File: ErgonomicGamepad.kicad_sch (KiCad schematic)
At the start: 68 parts, among them J1 USB_C_Receptacle_USB2.0_16P, J2 Conn_01x08, J3 Conn_01x08, J4 Conn_01x08, J5 AVR-ISP-6, J6 Conn_01x08, SW09 SW_DIP_x01, SW1 SW_DIP_x01, SW10 SW_DIP_x01, SW11 SW_DIP_x01, SW12 SW_DIP_x01, SW13 SW_DIP_x01, SW14 SW_DIP_x01, SW15 SW_DIP_x01, SW16 SW_DIP_x01, SW17 SW_DIP_x01, SW18 SW_DIP_x01, SW19 SW_DIP_x01, SW2 SW_DIP_x01, SW20 SW_DIP_x01, SW21 SW_DIP_x01, SW22 SW_DIP_x01, SW23 SW_DIP_x01, SW24 SW_DIP_x01, SW3 SW_DIP_x01, SW4 SW_DIP_x01, SW5 SW_DIP_x01, SW6 SW_DIP_x01, SW7 SW_DIP_x01, SW8 SW_DIP_x01, U1 ATmega32U4-A, Y1 Crystal

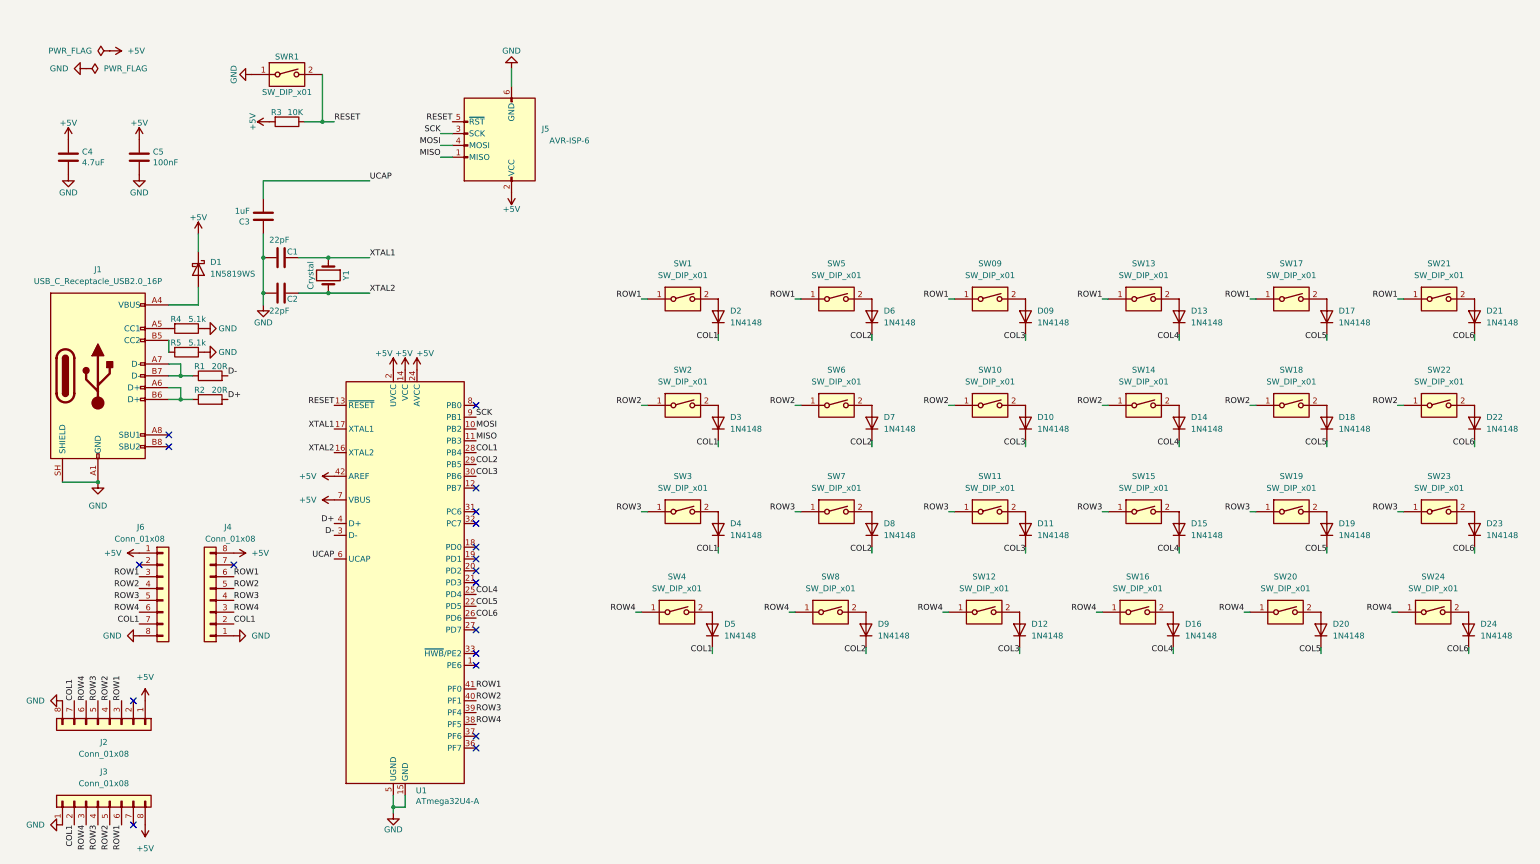
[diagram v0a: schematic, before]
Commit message: Assign footprints, fix RESET wiring, select JLCPCB as vendor
- Selected JLCPCB (+ LCSC parts catalog) as fabrication/assembly vendor
- Assigned footprints to 82 of 83 components (all but SWR1 reset
  switch, pending real pad dimensions from its datasheet): hotswap
  Kailh sockets for SW1-24 via the kiswitch library, HRO USB-C
  receptacle for J1, and stock KiCad footprints for the remaining
  resistors, caps, LEDs, test points, headers, jumper, and crystal
- Fixed RESET net: SWR1, J5 pin 5, and U1 pin 13 were previously
  disconnected/mislabeled (RESET and MOSI swapped on the ISP header,
  U1's reset pin floating); now correctly tied together
- Corrected README status claims that didn't match the actual
  schematic state, and documented remaining known issues (ISP
  MISO/SCK/MOSI not wired to the MCU's real SPI pins) plus the
  planned matrix pin re-layout to resolve it
- Ignore local Claude Code config and generated JLCPCB fabrication
  output

Co-Authored-By: Claude Sonnet 5 <noreply@anthropic.com>
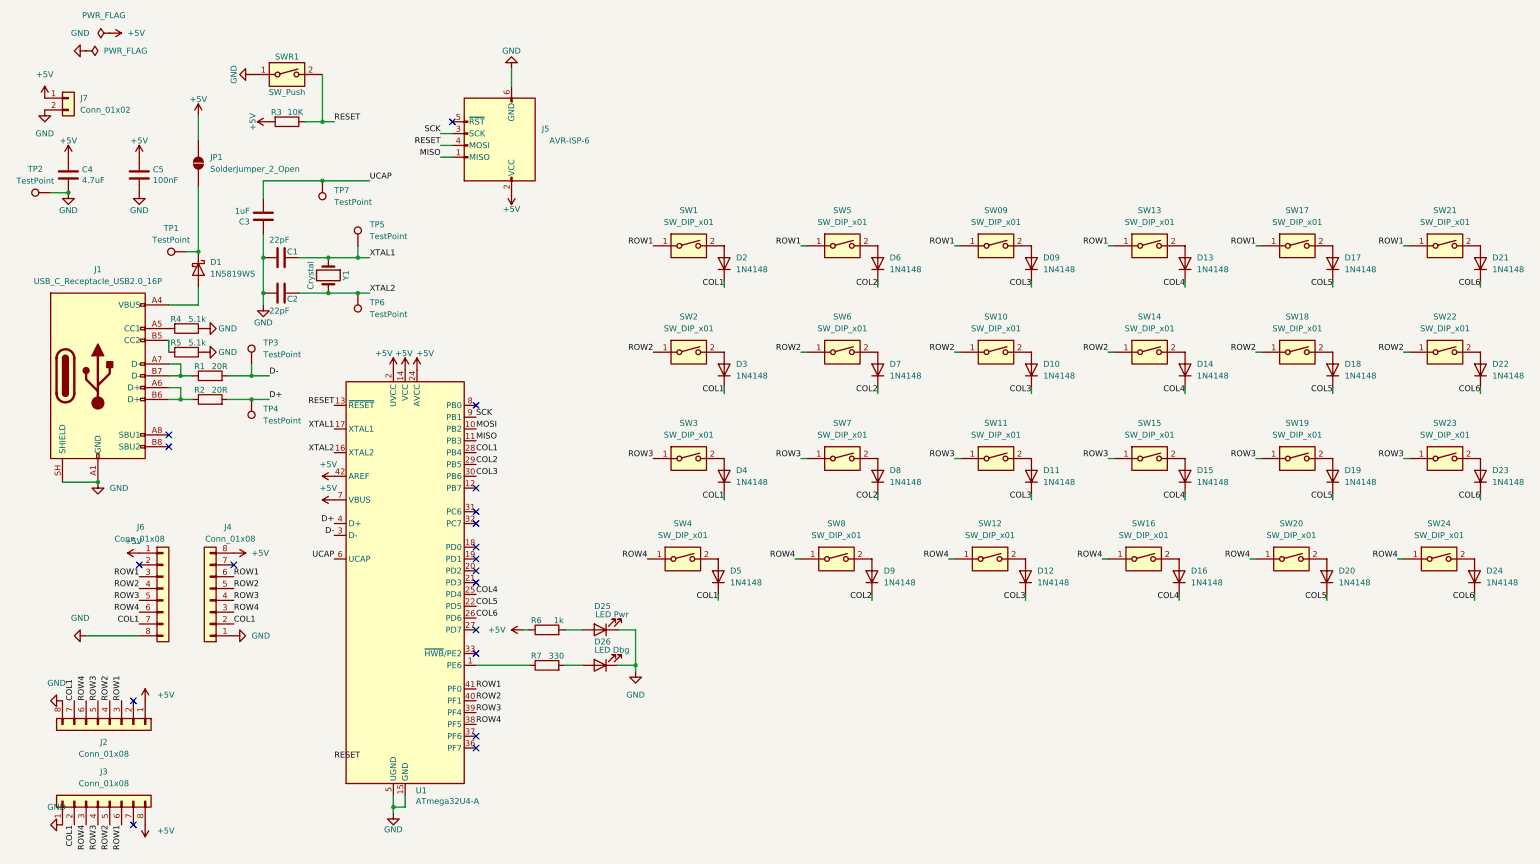
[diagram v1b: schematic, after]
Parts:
- added D25: LED Pwr, LED_SMD:LED_0603_1608Metric, symbol Device:LED
- added D26: LED Dbg, LED_SMD:LED_0603_1608Metric, symbol Device:LED
- added J7: Conn_01x02, Connector_PinHeader_2.54mm:PinHeader_1x02_P2.54mm_Vertical, symbol Connector_Generic:Conn_01x02
- added JP1: SolderJumper_2_Open, Jumper:SolderJumper-2_P1.3mm_Open_Pad1.0x1.5mm, symbol Jumper:SolderJumper_2_Open
- added R6: 1k, Resistor_SMD:R_0603_1608Metric, symbol Device:R
- added R7: 330, Resistor_SMD:R_0603_1608Metric, symbol Device:R
- added TP1, TP2, TP3, TP4, TP5, TP6, TP7: TestPoint, TestPoint:TestPoint_Pad_D1.5mm, symbol Connector:TestPoint
- J1: footprint Connector_USB:USB_C_Receptacle_Hirose_DX07S016HJ1R400 -> Connector_USB:USB_C_Receptacle_HRO_TYPE-C-31-M-12
- SW09, SW1, SW10, SW11, SW12, SW13, SW14, SW15, SW16, SW17, SW18, SW19, SW2, SW20, SW21, SW22, SW23, SW24, SW3, SW4, SW5, SW6, SW7, SW8: footprint Button_Switch_Keyboard:SW_Cherry_MX_1.00u_PCB -> Switch_Keyboard_Hotswap_Kailh:SW_Hotswap_Kailh_MX_Plated_1.00u
- SWR1: value SW_DIP_x01 -> SW_Push; footprint Button_Switch_Keyboard:SW_Cherry_MX_1.00u_PCB -> (none)
- Y1: footprint Crystal:Crystal_SMD_2016-4Pin_2.0x1.6mm -> Crystal:Crystal_SMD_3225-4Pin_3.2x2.5mm
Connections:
- net +5V: now also J7.1 (Pin_1), JP1.2 (B), R6.1; no longer D1.1 (K)
- net D+: now also TP4.1
- net D-: now also TP3.1
- net GND: now also D25.1 (K), D26.1 (K), J7.2 (Pin_2), TP2.1
- net MOSI: no longer J5.4 (MOSI)
- net RESET: now also J5.4 (MOSI); no longer J5.5 (~{RST})
- net UCAP: now also TP7.1
- net XTAL1: now also TP5.1
- net XTAL2: now also TP6.1
- net at U1.1 (PE6): now also R7.1
- new net: D1.1 (K), JP1.1 (A), TP1.1
- new net: D25.2 (A), R6.2
- new net: D26.2 (A), R7.2
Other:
- moved on the sheet: C4, C5, D09, D10, D11, D12, D13, D14, D15, D16, D17, D18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

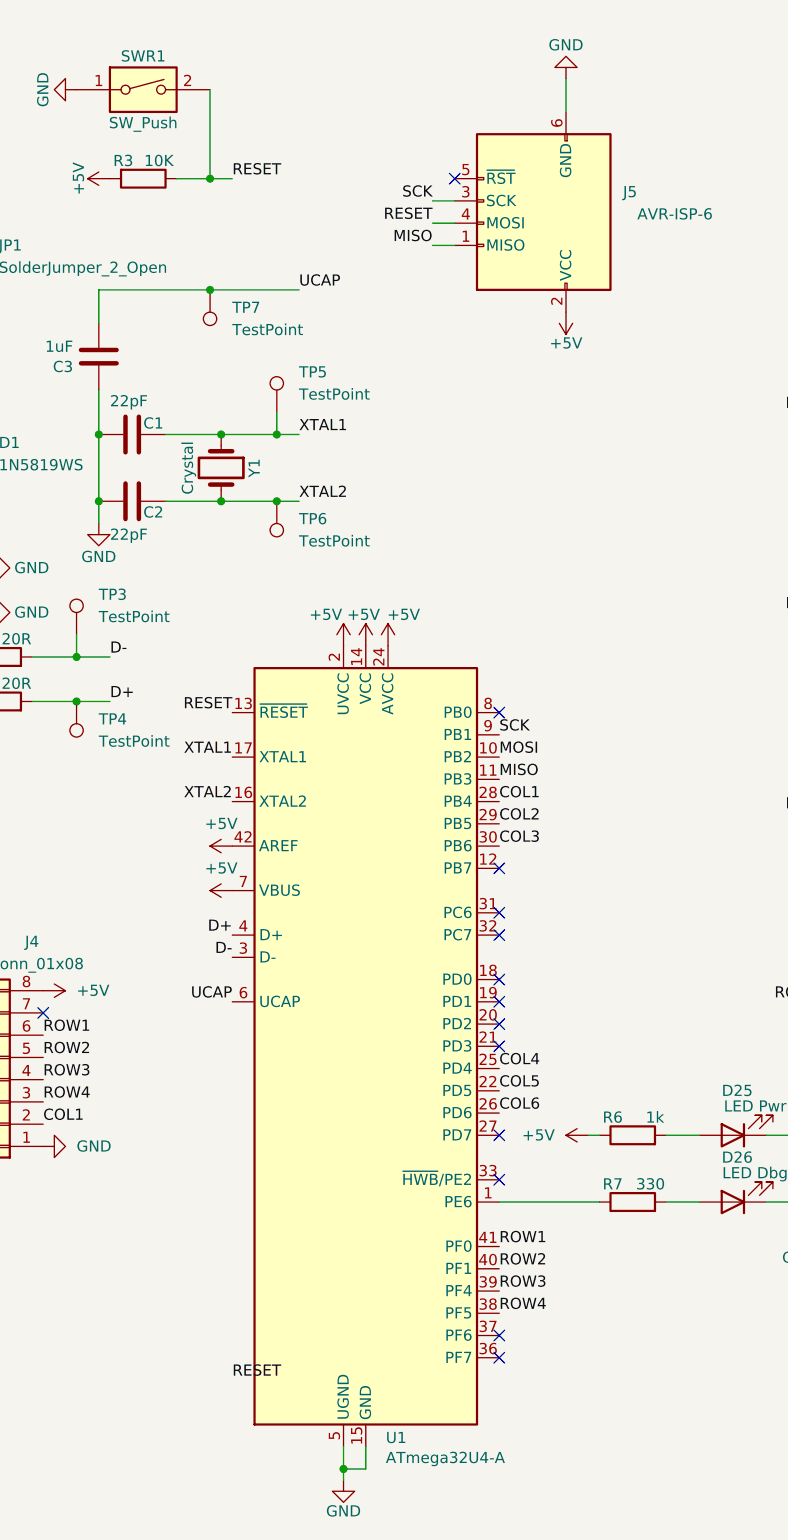
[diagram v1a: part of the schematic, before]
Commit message: Move ROW1-4 matrix pins from Port B to Port F, fix ISP RESET/MOSI swap
J5 pin 4 (physical MOSI) was wired to the RESET net while pin 5
(physical RST) was left no_connect; swapped so RST carries reset
and MOSI is properly no_connect until the SPI pins are wired.

ROW1-4 moved off PB6/PB5/PB4/PB3 onto PF0/PF1/PF4/PF5, freeing
PB1-PB6 for the planned ISP SCK/MOSI/MISO wiring. Removed the
stale SCK/MISO labels that were left on PF5/PF7 from the old
matrix layout. COL1-6 remain on PD1-PD6, unchanged.

Also adds a verification checklist to the README for re-running
ERC/DRC after pin remaps.

Co-Authored-By: Claude Sonnet 5 <noreply@anthropic.com>
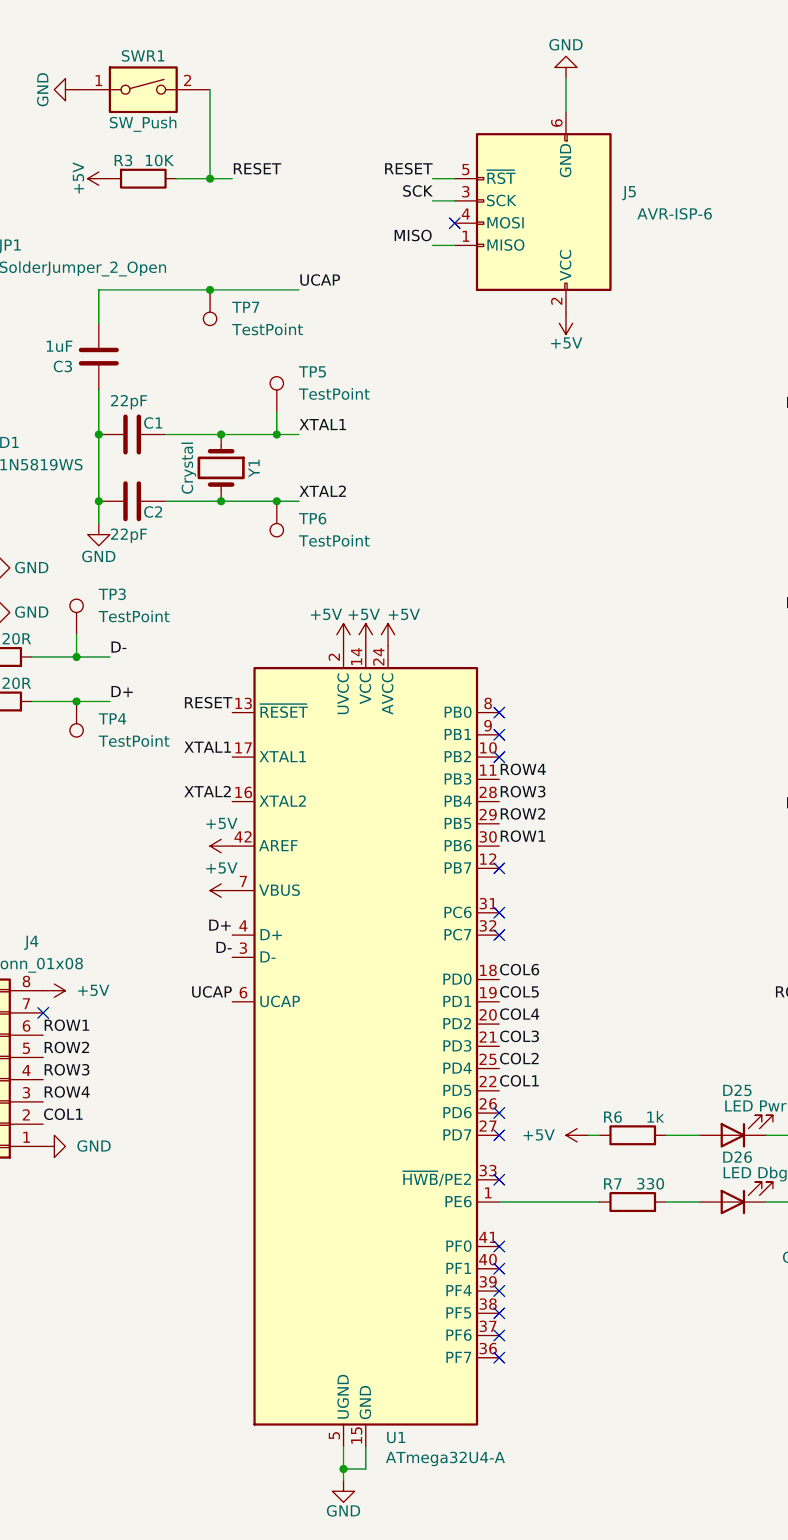
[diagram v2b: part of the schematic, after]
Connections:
- net COL1: now also U1.22 (PD5); no longer U1.28 (PB4)
- net COL2: now also U1.25 (PD4); no longer U1.29 (PB5)
- net COL3: now also U1.21 (PD3); no longer U1.30 (PB6)
- net COL4: now also U1.20 (PD2); no longer U1.25 (PD4)
- net COL5: now also U1.19 (PD1); no longer U1.22 (PD5)
- net COL6: now also U1.18 (PD0); no longer U1.26 (PD6)
- net MISO: no longer U1.11 (PB3)
- net RESET: now also J5.5 (~{RST}); no longer J5.4 (MOSI)
- net ROW1: now also U1.30 (PB6); no longer U1.41 (PF0)
- net ROW2: now also U1.29 (PB5); no longer U1.40 (PF1)
- net ROW3: now also U1.28 (PB4); no longer U1.39 (PF4)
- net ROW4: now also U1.11 (PB3); no longer U1.38 (PF5)
- net SCK: no longer U1.9 (PB1)
- net MOSI: no longer names the net of U1.10 (PB2)
- no-connect marks 19 -> 22
